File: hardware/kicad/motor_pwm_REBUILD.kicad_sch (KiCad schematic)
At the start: 29 parts, among them J101 24V_IN, J102 MOTOR_24V_125W, J103 LOGIC_3V3_IN, J104 INTERNAL_MAIN_SOURCE_PORT_FAN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, Q101 IRFB4110PBF (100V; RDS(on) @ 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, U9001 LTC7001IMSE#PBF; MSOP-10 EP, U9002 INA240A1ID, U9003 LMV331M5X/NOPB, U9004 SN74LVC1G32DBVR, U9005 SN74LVC1G08DBVR, U9006 SN74LVC1G08DBVR, U9007 LM317HVT/NOPB TO-220; TJ 0…12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

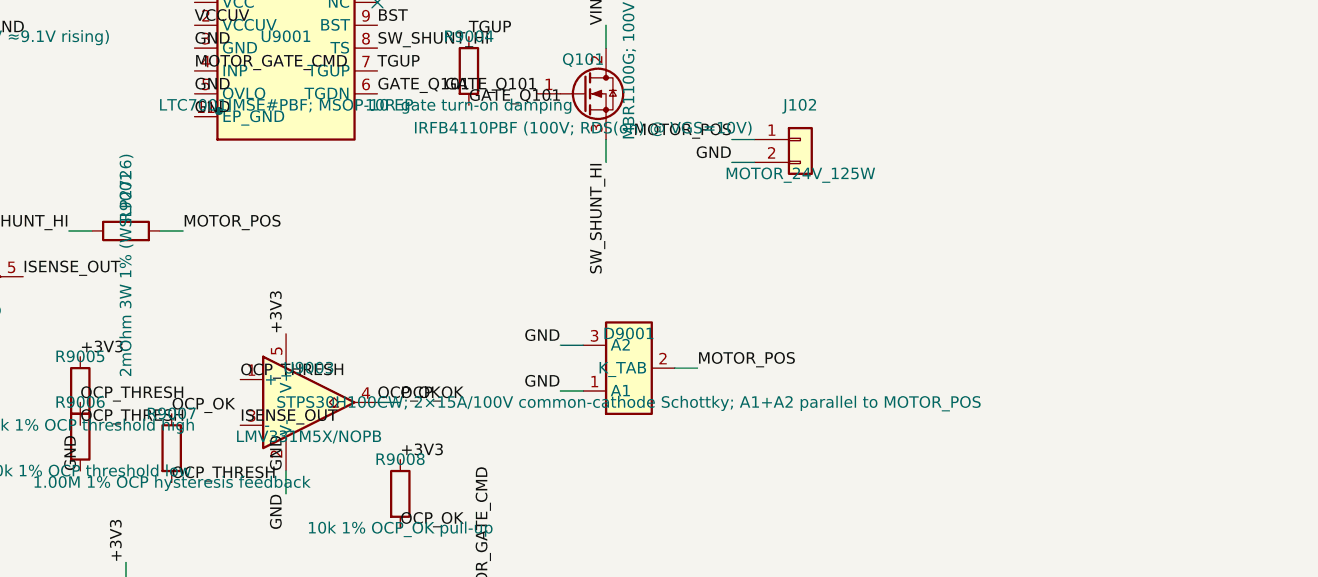
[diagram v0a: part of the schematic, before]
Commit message: hardware: WIP correct TVS and relay decisions and motor labels
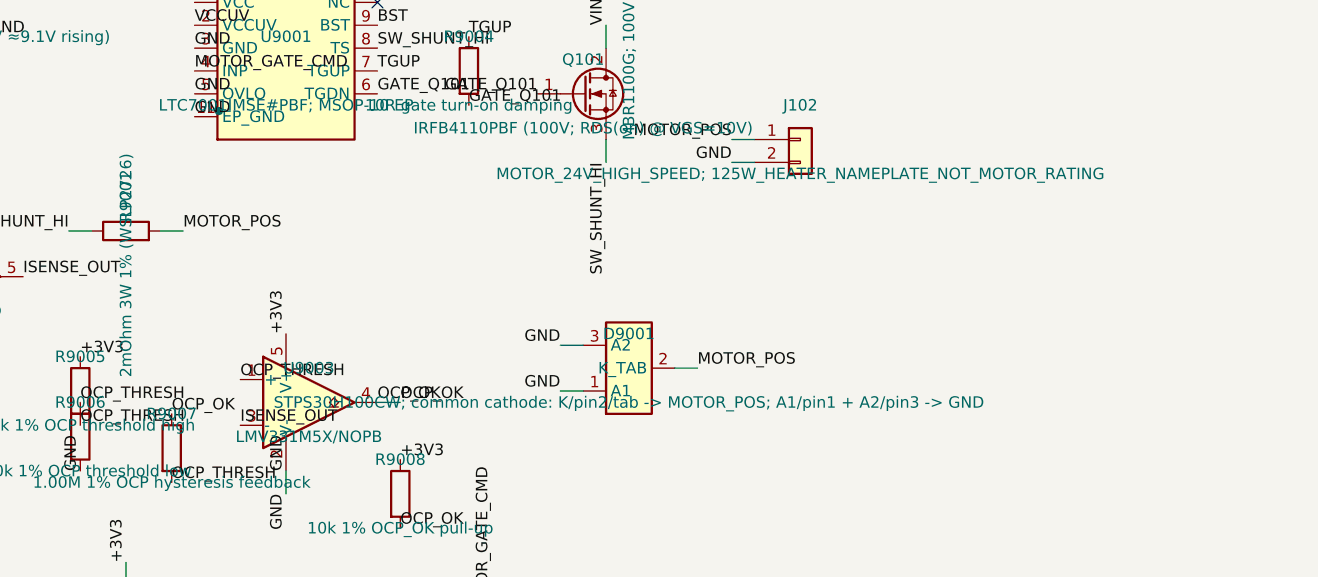
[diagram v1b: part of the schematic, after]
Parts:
- D9001: value STPS30H100CW; 2×15A/100V common-cathode Schottky; A1+A2 parallel to MOTOR_POS -> STPS30H100CW; common cathode: K/pin2/tab -> MOTOR_POS; A1/pin1 + A2/pin3 -> GND
- J102: value MOTOR_24V_125W -> MOTOR_24V_HIGH_SPEED; 125W_HEATER_NAMEPLATE_NOT_MOTOR_RATING
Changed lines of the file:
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@@
 		)
 	)
-	(property "Value" "MOTOR_24V_125W"
+	(property "Value" "MOTOR_24V_HIGH_SPEED; 125W_HEATER_NAMEPLATE_NOT_MOTOR_RATING"
 		(at 204.47 93.98 0)
 		(effects
@@
 		)
 	)
-	(property "Value" "STPS30H100CW; 2×15A/100V common-cathode Schottky; A1+A2 parallel to MOTOR_POS"
+	(property "Value" "STPS30H100CW; common cathode: K/pin2/tab -> MOTOR_POS; A1/pin1 + A2/pin3 -> GND"
 		(at 185.42 119.38 0)
 		(effects

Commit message: chore: consolidate current CAD project
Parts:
- removed D9002: MBR1100G; 100V 1A Schottky bootstrap diode, symbol Device:D_Schottky
- removed J101: 24V_IN, symbol Connector_Generic:Conn_01x02
- removed J103: LOGIC_3V3_IN, symbol Connector_Generic:Conn_01x03
- removed J104: INTERNAL_MAIN_SOURCE_PORT_FAN_3V3_GND_NOT_EXTERNA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, symbol Connector_Generic:Conn_01x03
- added C9011: 100nF X7R 16V 10%; U9005 local bypass, Sirokko_TFT_Passives:C_Murata_GRM188_1608_Reflow, symbol Device:C
- added C9012: 100nF X7R 16V 10%; U9006 local bypass, Sirokko_TFT_Passives:C_Murata_GRM188_1608_Reflow, symbol Device:C
- added D9002: MMBD1501A; 200V 200mA silicon low-leakage bootstr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, Package_TO_SOT_SMD:SOT-23, symbol Sirokko_Power:MMBD1501A_ON
- C9004, C9005, C9006: footprint (none) -> Sirokko_TFT_Passives:C_Murata_GRM188_1608_Reflow; MPN (none) -> GRM188R71C104KA01D; Manufacturer (none) -> Murata
- C9007: value 1uF X7R 25V; LTC7001 VCC local decoupling -> 1uF ±10% X7R 50V 0805; LTC7001 VCC local decoupling; footprint (none) -> Capacitor_SMD:C_0805_2012Metric; MPN (none) -> GRM21BR71H105KA12L
- C9008: value 1uF X7R 25V (BST-TS) -> 1uF ±10% X7R 50V 0805 (BST-TS); footprint (none) -> Capacitor_SMD:C_0805_2012Metric; MPN (none) -> GRM21BR71H105KA12L
- D9001: footprint (none) -> Package_TO_SOT_THT:TO-220-3_Vertical
- J102: footprint (none) -> TerminalBlock_Phoenix:TerminalBlock_Phoenix_MKDS-1,5-2-5.08_1x02_P5.08mm_Horizontal; MPN (none) -> 1715721
- Q101: footprint (none) -> Package_TO_SOT_THT:TO-220-3_Vertical; MPN (none) -> IRFB4110PBF
- R9001: value 2mOhm 3W 1% (WSLP2726) -> WSLP27262L000FEA; 2mOhm 1% 5W @70C; footprint (none) -> Sirokko_Power:WSLP2726; MPN (none) -> WSLP27262L000FEA
- R9002: footprint (none) -> Resistor_SMD:R_0603_1608Metric; MPN (none) -> RC0603FR-07100KL; Manufacturer (none) -> YAGEO
- R9003: footprint (none) -> Resistor_SMD:R_0603_1608Metric; MPN (none) -> RC0603FR-07130KL; Manufacturer (none) -> YAGEO
- R9004: footprint (none) -> Resistor_SMD:R_0603_1608Metric; MPN (none) -> RC0603FR-0710RL
- R9005: footprint (none) -> Resistor_SMD:R_0603_1608Metric; MPN (none) -> RC0603FR-0730K1L
- R9006, R9008: footprint (none) -> Resistor_SMD:R_0603_1608Metric; MPN (none) -> RC0603FR-0710KL; Manufacturer (none) -> YAGEO
- R9007: footprint (none) -> Resistor_SMD:R_0603_1608Metric; MPN (none) -> RC0603FR-071ML; Manufacturer (none) -> YAGEO
- R9009: footprint (none) -> Resistor_SMD:R_0805_2012Metric; MPN (none) -> RC0805FR-0775RL; Manufacturer (none) -> YAGEO; Supplier_PN (none) -> ChipDip 8001791959; Supplier_URL (none) -> https://www.chipdip.ru/product/rc0805fr-0775rl-yageo-800179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
- R9010: value 681R 1% 0.5W; LM317 ADJ→GND -> 681R 1% 0.75W; LM317 ADJ→GND; footprint (none) -> Resistor_SMD:R_2010_5025Metric; MPN (none) -> RC2010FK-07681RL; Manufacturer (none) -> YAGEO; Supplier_PN (none) -> ChipDip 8031324009; Supplier_URL (none) -> https://www.chipdip.ru/product/rc2010fk-07681rl-thick-film-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
- U9001: footprint (none) -> Package_SO:MSOP-10-1EP_3x3mm_P0.5mm_EP1.68x1.88mm; MPN (none) -> LTC7001IMSE#PBF
- U9002: footprint (none) -> Package_SO:SOIC-8_3.9x4.9mm_P1.27mm; MPN (none) -> INA240A1ID
- U9003: value LMV331M5X/NOPB -> TLV9020DBVR; footprint (none) -> Package_TO_SOT_SMD:SOT-23-5; symbol Comparator:LMV331 -> Sirokko_Power:TLV9020DBVR; MPN (none) -> TLV9020DBVR
- U9004: footprint (none) -> Package_TO_SOT_SMD:SOT-23-5; MPN (none) -> SN74LVC1G32DBVR
- U9005, U9006: footprint (none) -> Package_TO_SOT_SMD:SOT-23-5; MPN (none) -> SN74LVC1G08DBVR
- U9007: footprint (none) -> Package_TO_SOT_THT:TO-220-3_Vertical; MPN (none) -> LM317HVT/NOPB
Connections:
- net FAN_EMERG_3V3 is gone; now on net GND: U9004.2
- net +3V3: now also C9011.1, C9012.1
- net BST: now also D9002.3 (K)
- net GND: now also C9011.2, C9012.2
- net VDRV12V: now also D9002.1 (A)
- net FAN_CMD renamed FAN_REQUEST
- net PWM_SPEED_CMD renamed SPEED_CMD
- net VIN_RAW_18_30V renamed P24_PROTECTED
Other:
- note added: "CURRENT INTERFACE - DRAFT: 15 A continuous design limit, not measured motor current. Logic design range +3V3=3.135...3.465 V; 3.0...3.6 V is an additional stress calculation. Nominal ideal OCP at 3.3 V: trip 21.081 A, reset 20.471 A. These are NOT qualified limits. See OCP_TLV9020_REVIEW_RU.md and ocp_threshold_model.json for assumptions. Coordinate branch fuse, wiring, connector, MOSFET SOA and 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"
- note added: "LOGIC CONTRACT - DRAFT, not bench qualified. INP = ((FAN_CMD AND PWM_SPEED_CMD) OR FAN_EMERG_3V3) AND OCP_OK. R9002=100k pulls INP LOW when +3V3/gates are off; VIN/VDRV may remain. U9003 TLV9020DBVR: open-drain OUT4; IN+1, IN-3, V-2, V+5. Overcurrent pulls OCP_OK LOW and inhibits both PWM and emergency command. Verify physical shutdown timing and current decay on a safe bench."
- note removed: "CURRENT INTERFACE: design continuous limit 15 A; comparator trip/release corridor 19.11…22.42 A for +3V3=3.135…3.465 V and 1% resistors. This is hardware turn-off, not a current regulator. External branch fuse/wiring/connector must be selected for the 15 A continuous interface; motor L/I/start profile remains a commissioning measurement."
- note removed: "QUALIFIED LOGIC: INP = ((FAN_CMD AND PWM_SPEED_CMD) OR FAN_EMERG_3V3) AND OCP_OK. R9002=100k pulls INP low. Loss of +3V3 drives gates Hi-Z; R9002 forces LTC7001 INP=LOW even with VIN/VDRV alive. OCP_OK is LMV331 open collector: overcurrent pulls LOW and therefore turns OFF both PWM and emergency command."

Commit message: WIP: publish current unfinished CAD sources
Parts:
- D9001: footprint Package_TO_SOT_THT:TO-220-3_Vertical -> Sirokko_Power:TO-247-3_Vertical_STPS30H100CW_Drill2.2mm
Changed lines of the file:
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@@
 		)
 	)
-	(property "Footprint" "Package_TO_SOT_THT:TO-220-3_Vertical"
+	(property "Footprint" "Sirokko_Power:TO-247-3_Vertical_STPS30H100CW_Drill2.2mm"
 		(at 185.42 115.57 0)
 		(effects

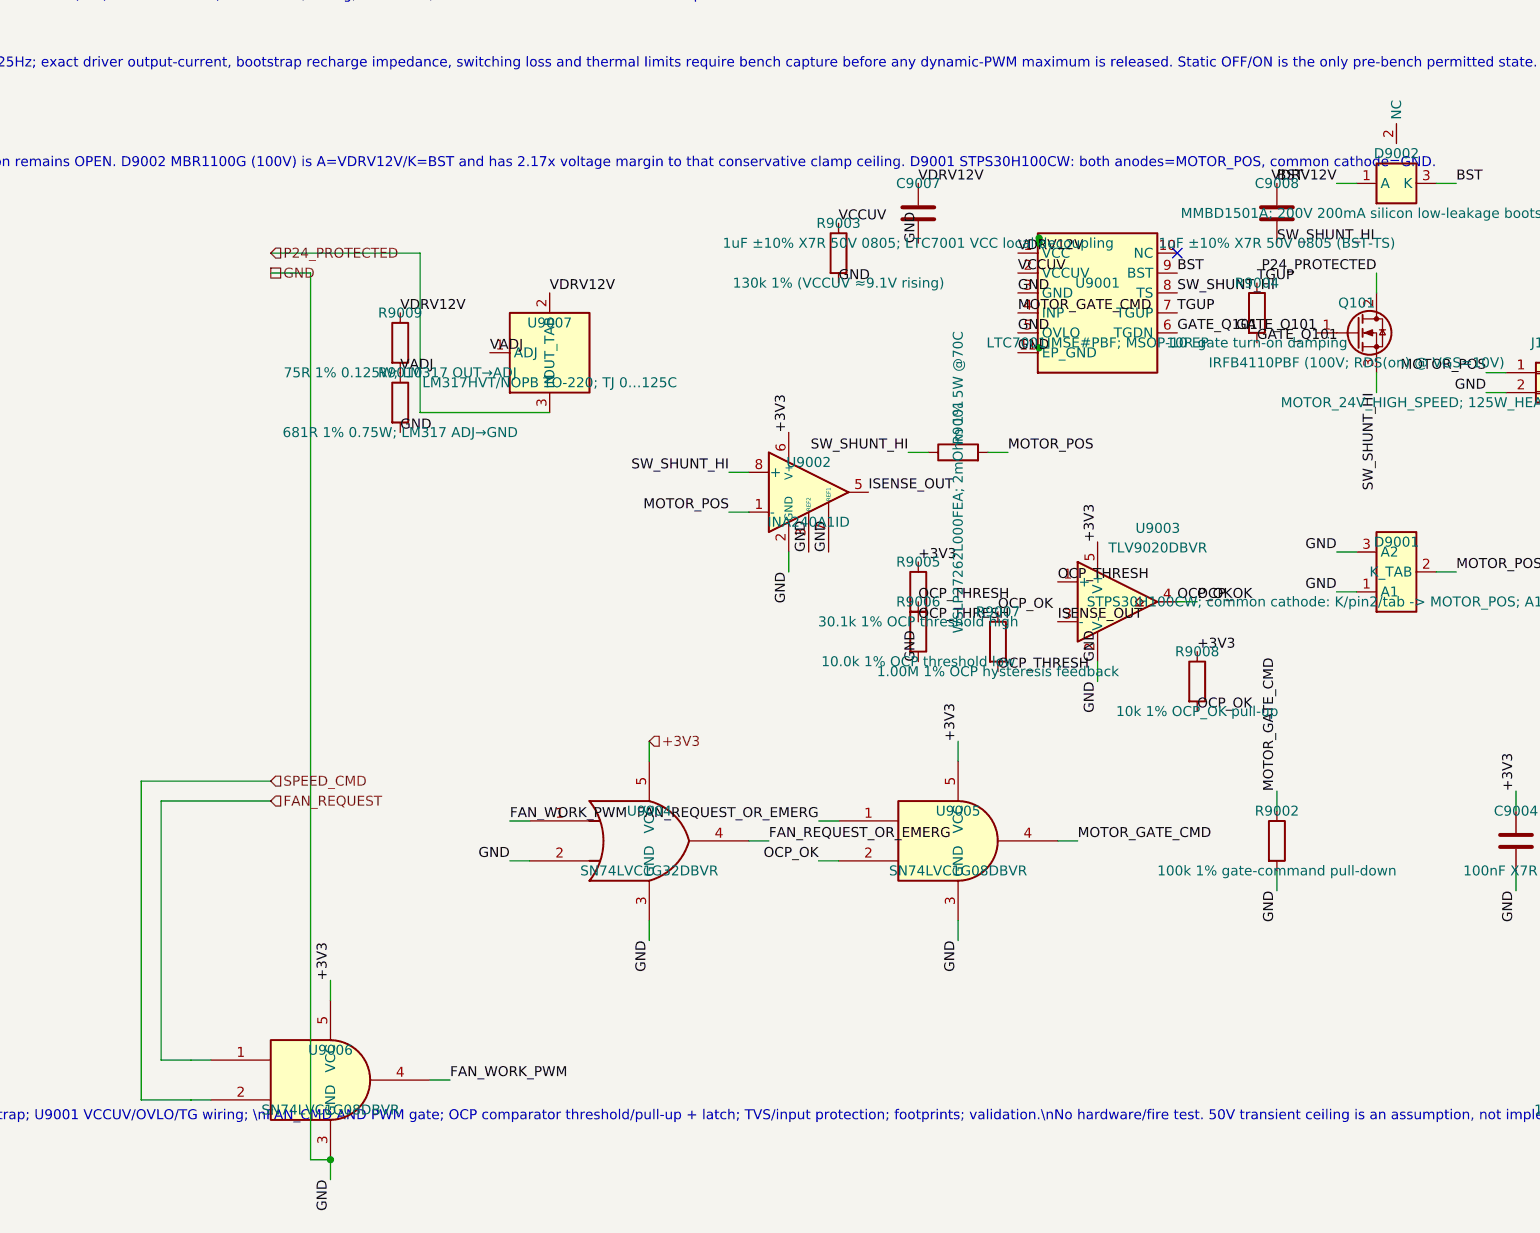
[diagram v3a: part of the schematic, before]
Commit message: Mark R9001 Kelvin pads as jumpers
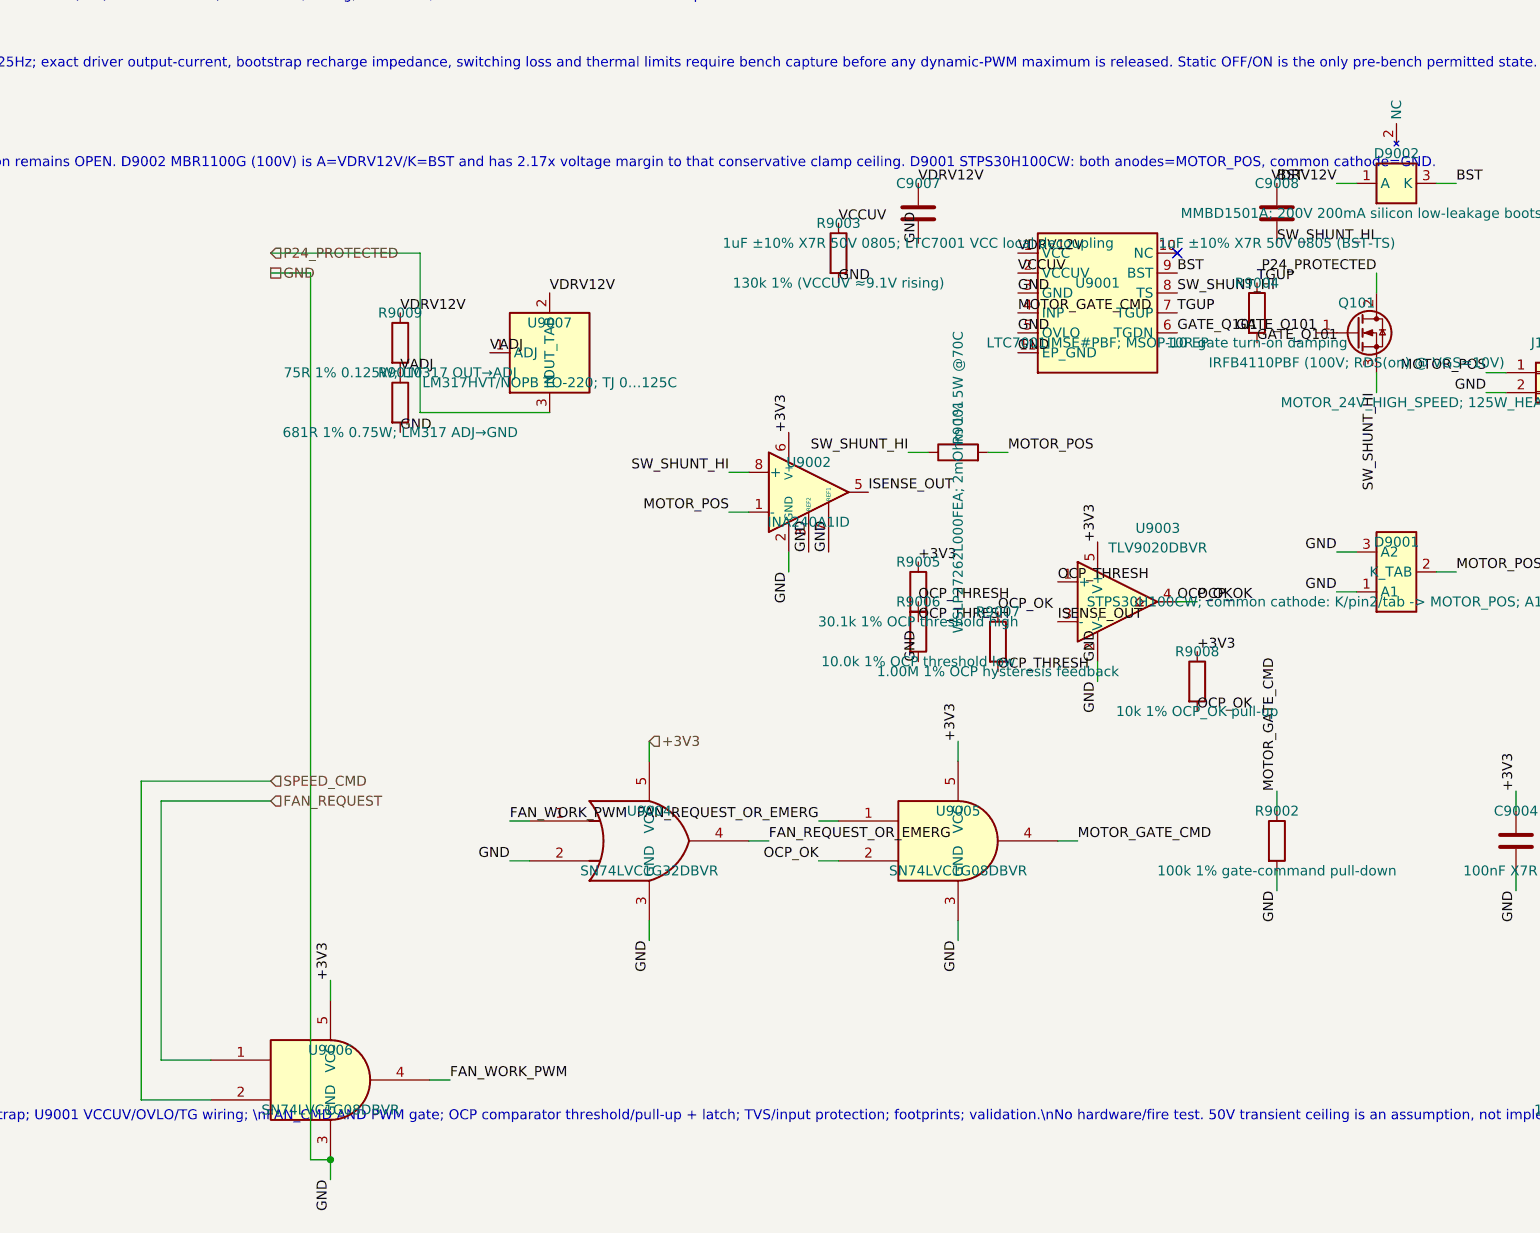
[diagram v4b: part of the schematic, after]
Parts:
- R9001: symbol Device:R -> Sirokko_Power:WSLP2726_Kelvin

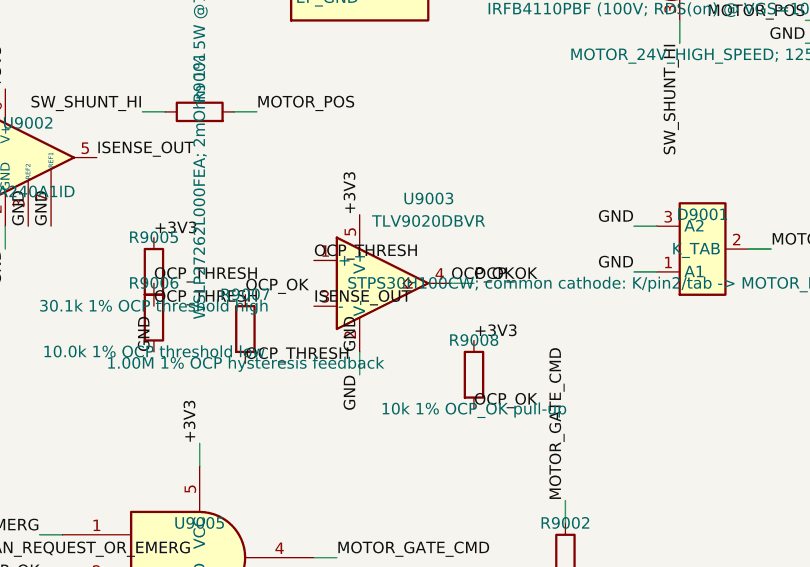
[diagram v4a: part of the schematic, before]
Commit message: WIP: connect OCP_OK feedback to GPIO18
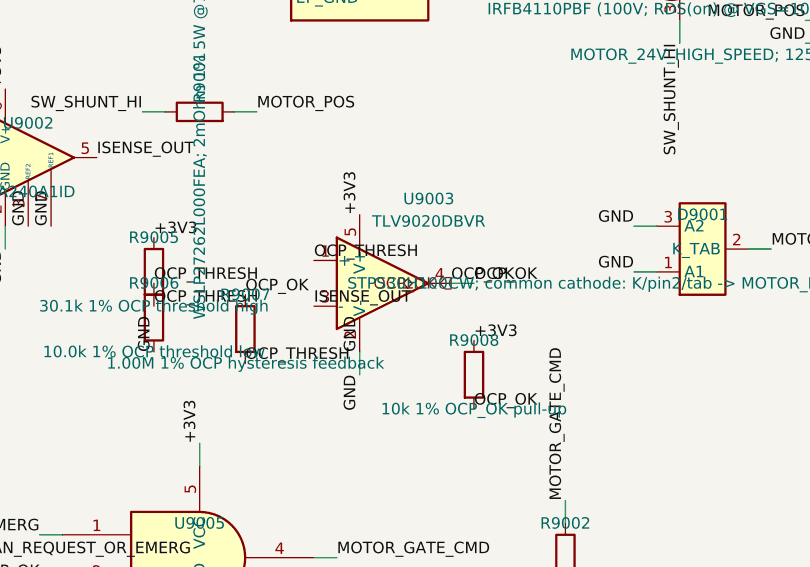
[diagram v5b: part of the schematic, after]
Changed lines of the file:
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@@
+		)
+	)
+	(hierarchical_label "OCP_OK"
+		(shape output)
+		(at 157.48 119.38 180)
+		(effects
+			(font
+				(size 1.27 1.27)
+			)
+			(justify right)
 		)
 	)
